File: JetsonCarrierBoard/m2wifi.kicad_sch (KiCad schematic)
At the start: 10 parts

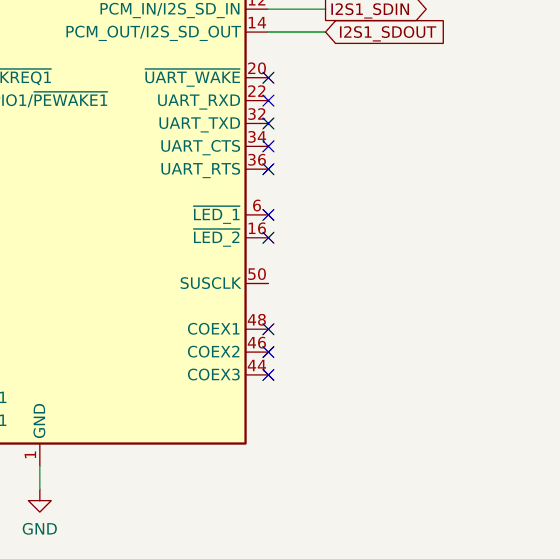
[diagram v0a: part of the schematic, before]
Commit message: IMU wiring
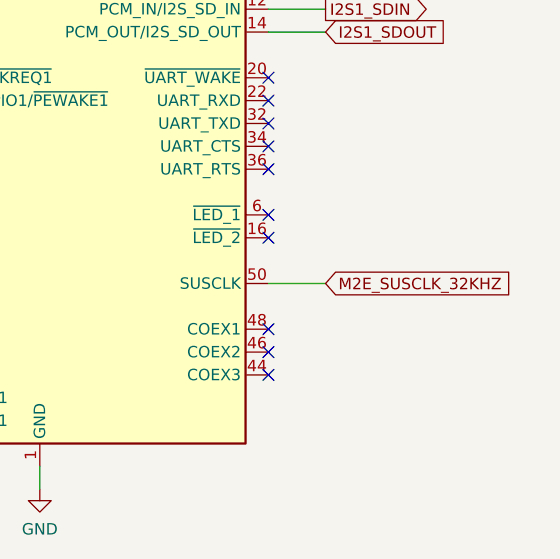
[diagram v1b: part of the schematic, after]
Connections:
- net M2E_SUSCLK_32KHZ: now reaches J?.50 (SUSCLK)
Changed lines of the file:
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@@
+    (stroke (width 0) (type default) (color 0 0 0 0))
+  )
+  (wire (pts (xy 173.99 125.73) (xy 180.34 125.73))
     (stroke (width 0) (type default) (color 0 0 0 0))
   )
@@
     )
   )
+  (global_label "M2E_SUSCLK_32KHZ" (shape input) (at 180.34 125.73 0) (fields_autoplaced)
+    (effects (font (size 1.27 1.27)) (justify left))
+    (property "Intersheet References" "${INTERSHEET_REFS}" (id 0) (at 202.045 125.6506 0)
+      (effects (font (size 1.27 1.27)) (justify left) hide)
+    )
+  )

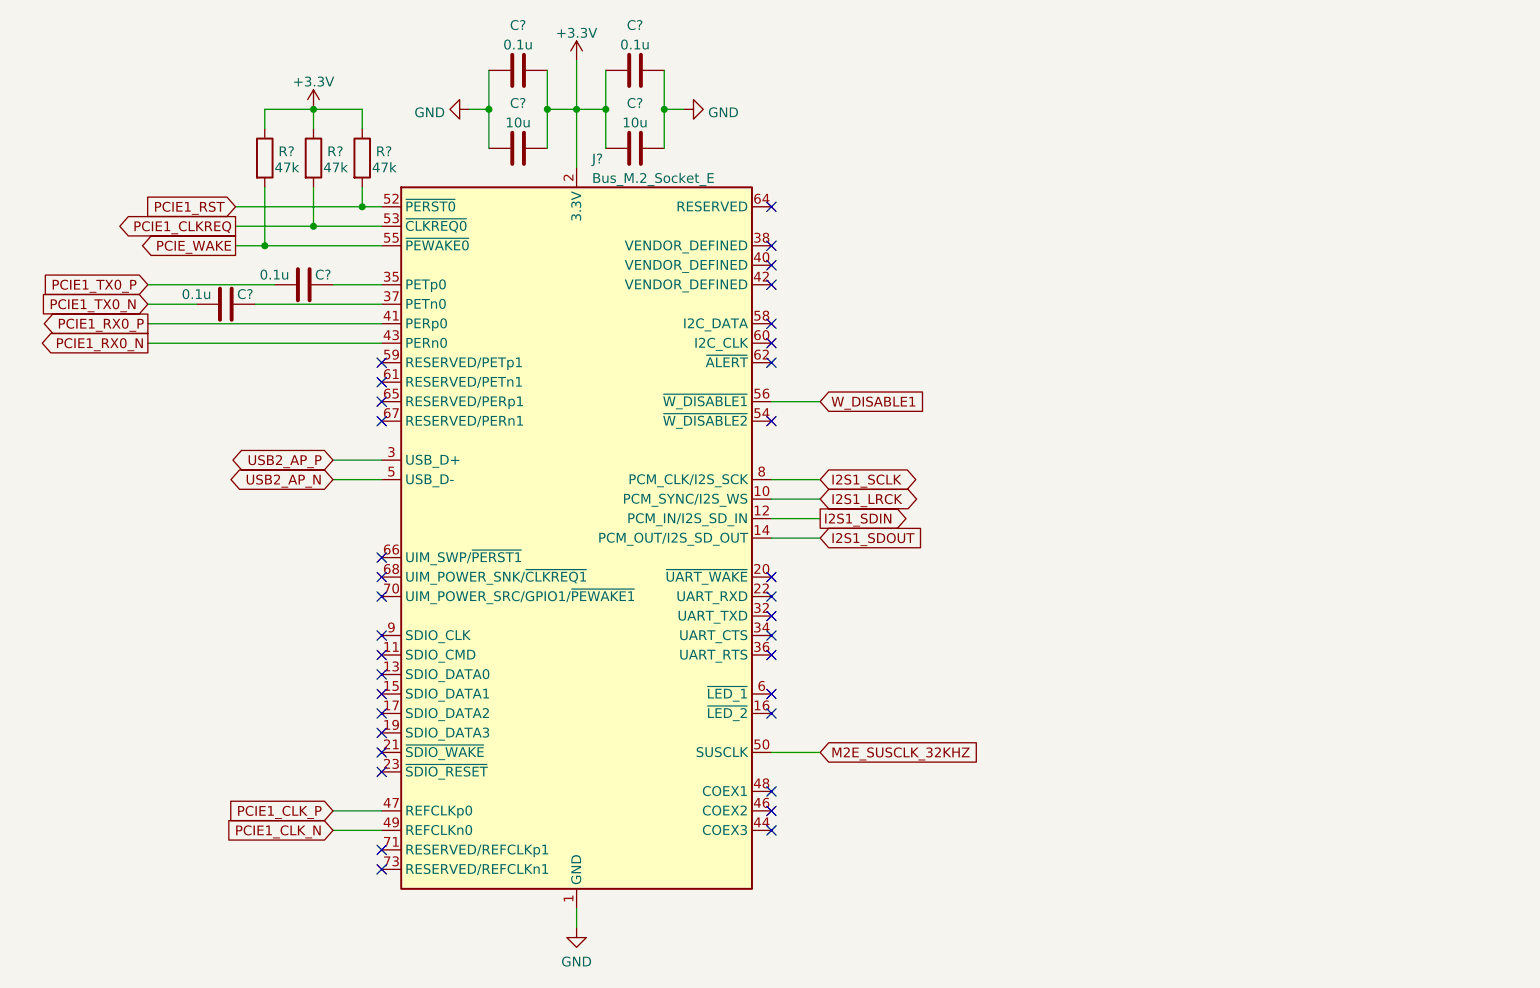
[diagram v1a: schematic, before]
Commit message: Added basic circuits, LED circuit, GPIO pins in GPIO page
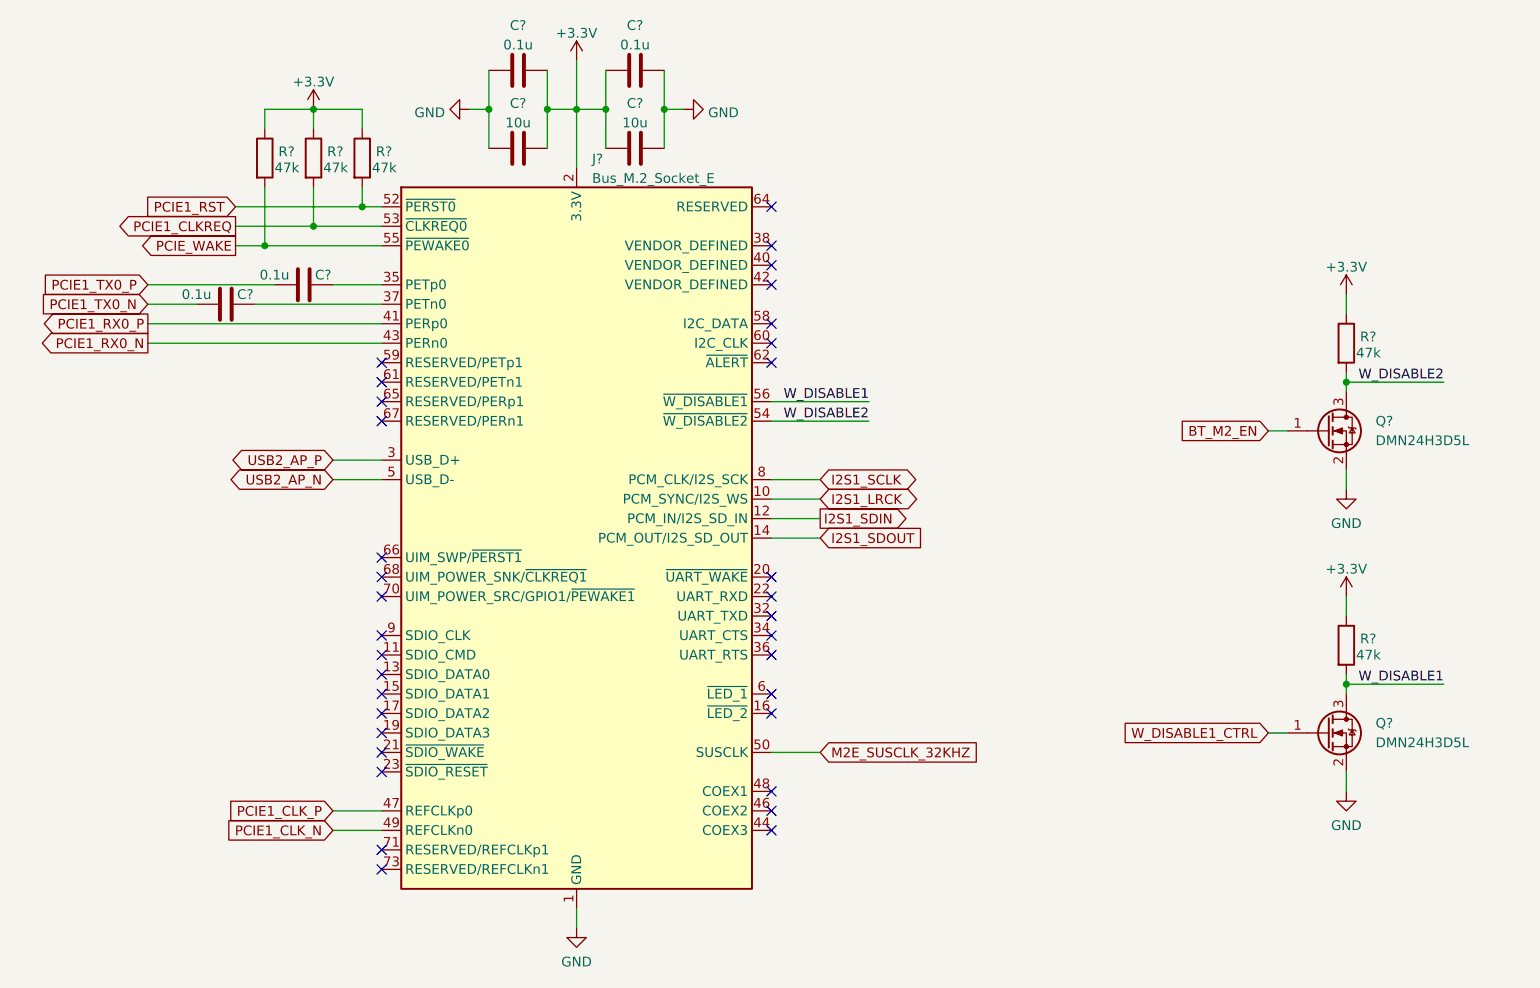
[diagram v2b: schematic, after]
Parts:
- added Q? (x2): DMN24H3D5L, Package_TO_SOT_SMD:SOT-23, symbol Transistor_FET:DMN24H3D5L
- added R? (x2): 47k, symbol Device:R
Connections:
- net +3V3: now also R?.1, R?.1
- net GND: now also Q?.2 (S), Q?.2 (S)
- net W_DISABLE1: now also Q?.3 (D), R?.2
- net W_DISABLE2: now reaches J?.54 (~{W_DISABLE2})
- net W_DISABLE2: now also Q?.3 (D), R?.2
- new net BT_M2_EN: Q?.1 (G)
- new net W_DISABLE1_CTRL: Q?.1 (G)
- no-connect marks 35 -> 34

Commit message: Adding more Title block info and changing main hierarchical page layout
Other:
- title: (none) -> M.2 WiFi (Key E)
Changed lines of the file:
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@@
 (kicad_sch (version 20211123) (generator eeschema)
   (paper "A4")
+  (title_block
+    (title "M.2 WiFi (Key E)")
+    (date "2022-09-18")
+    (rev "1.0")
+  )
   (junction (at 137.16 41.91) (diameter 0) (color 0 0 0 0)
   )

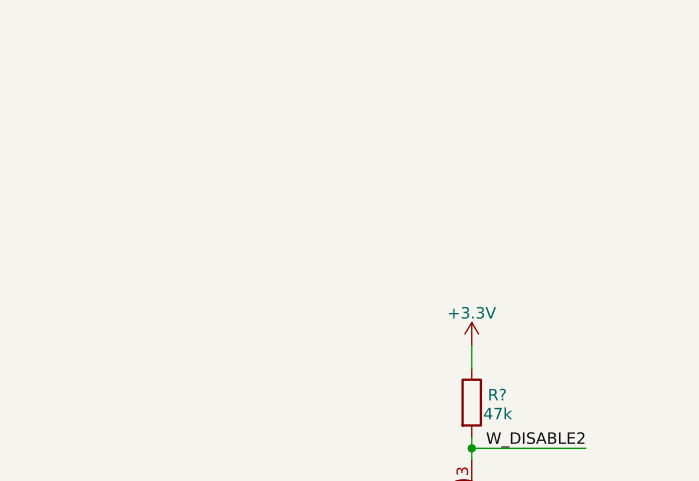
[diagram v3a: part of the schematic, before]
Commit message: Improvement list, fixes, and readability improvements
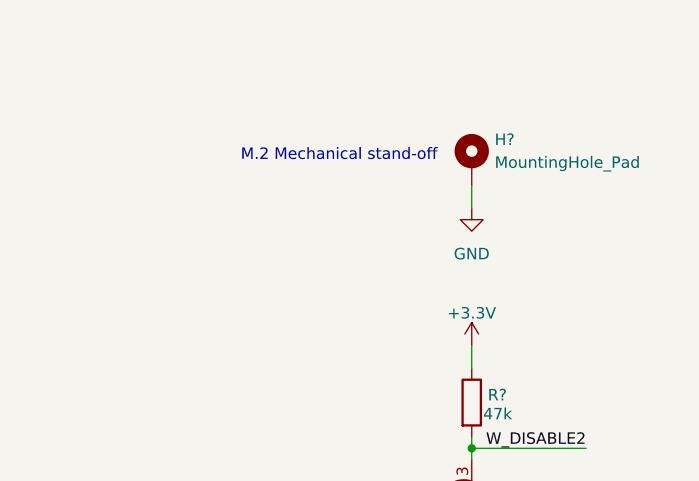
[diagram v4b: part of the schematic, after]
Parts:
- added H?: MountingHole_Pad, symbol Mechanical:MountingHole_Pad
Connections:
- net GND: now also H?.1
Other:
- note added: "M.2 Mechanical stand-off"
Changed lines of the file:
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@@
   (junction (at 107.95 59.69) (diameter 0) (color 0 0 0 0)
   )
+  (no_connect (at 173.99 102.87))
   (no_connect (at 123.19 140.97))
   (no_connect (at 123.19 138.43))
@@
   (no_connect (at 173.99 72.39))
   (no_connect (at 173.99 69.85))
-  (no_connect (at 173.99 102.87))
   (no_connect (at 173.99 105.41))
   (no_connect (at 173.99 107.95))
@@
     (stroke (width 0) (type default) (color 0 0 0 0))
   )
+  (wire (pts (xy 248.92 48.26) (xy 248.92 50.8))
+    (stroke (width 0) (type default) (color 0 0 0 0))
+  )
   (wire (pts (xy 173.99 95.25) (xy 180.34 95.25))
     (stroke (width 0) (type default) (color 0 0 0 0))
@@
   (wire (pts (xy 134.62 41.91) (xy 137.16 41.91))
     (stroke (width 0) (type default) (color 0 0 0 0))
+  )
+  (text "M.2 Mechanical stand-off" (at 245.11 45.72 180)
+    (effects (font (size 1.27 1.27)) (justify right bottom))
   )
   (label "W_DISABLE2" (at 261.62 77.47 180)
@@
     )
     (property "Datasheet" "" (id 3) (at 248.92 105.41 0)
+      (effects (font (size 1.27 1.27)) hide)
+    )
+    (pin "1")
+  )
+  (symbol (lib_id "power:GND") (at 248.92 50.8 0) (unit 1)
+    (in_bom yes) (on_board yes) (fields_autoplaced)
+    (property "Reference" "#PWR?" (id 0) (at 248.92 57.15 0)
+      (effects (font (size 1.27 1.27)) hide)
+    )
+    (property "Value" "GND" (id 1) (at 248.92 55.88 0))
+    (property "Footprint" "" (id 2) (at 248.92 50.8 0)
+      (effects (font (size 1.27 1.27)) hide)
+    )
+    (property "Datasheet" "" (id 3) (at 248.92 50.8 0)
       (effects (font (size 1.27 1.27)) hide)
     )
@@
     (pin "3")
   )
+  (symbol (lib_id "Mechanical:MountingHole_Pad") (at 248.92 45.72 0) (unit 1)
+    (in_bom yes) (on_board yes) (fields_autoplaced)
+    (property "Reference" "H?" (id 0) (at 251.46 43.1799 0)
+      (effects (font (size 1.27 1.27)) (justify left))
+    )
+    (property "Value" "MountingHole_Pad" (id 1) (at 251.46 45.7199 0)
+      (effects (font (size 1.27 1.27)) (justify left))
+    )
+    (property "Footprint" "" (id 2) (at 248.92 45.72 0)
+      (effects (font (size 1.27 1.27)) hide)
+    )
+    (property "Datasheet" "~" (id 3) (at 248.92 45.72 0)
+      (effects (font (size 1.27 1.27)) hide)
+    )
+    (pin "1")
+  )
   (symbol (lib_id "power:GND") (at 248.92 91.44 0) (unit 1)
